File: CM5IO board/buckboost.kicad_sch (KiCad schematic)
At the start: 14 parts, among them IC1 TPS61089RNRR

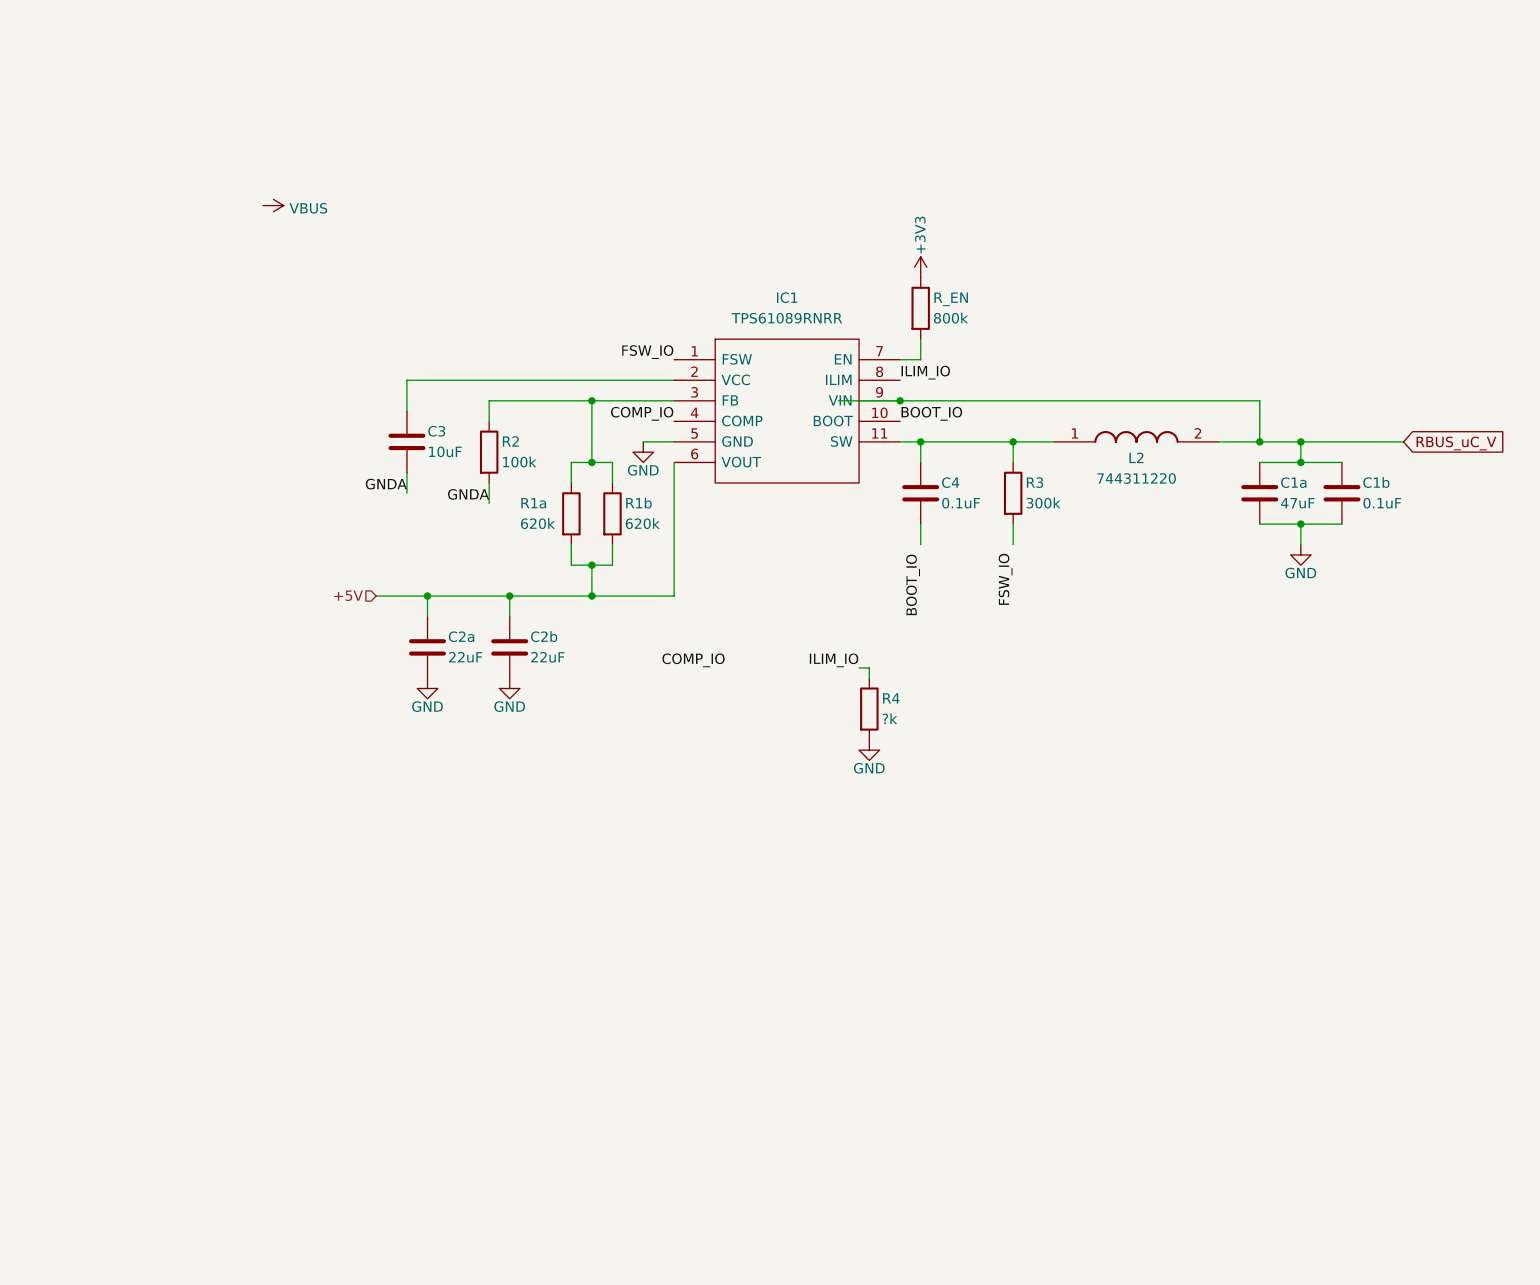
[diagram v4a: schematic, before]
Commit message: EN changed & finalised
Added MOSFET; using potential divider (i.e. R7//R8) EN switch is at 1.65V which is >1.2V from the data sheet. Added C7 to avoid voltage spikes.
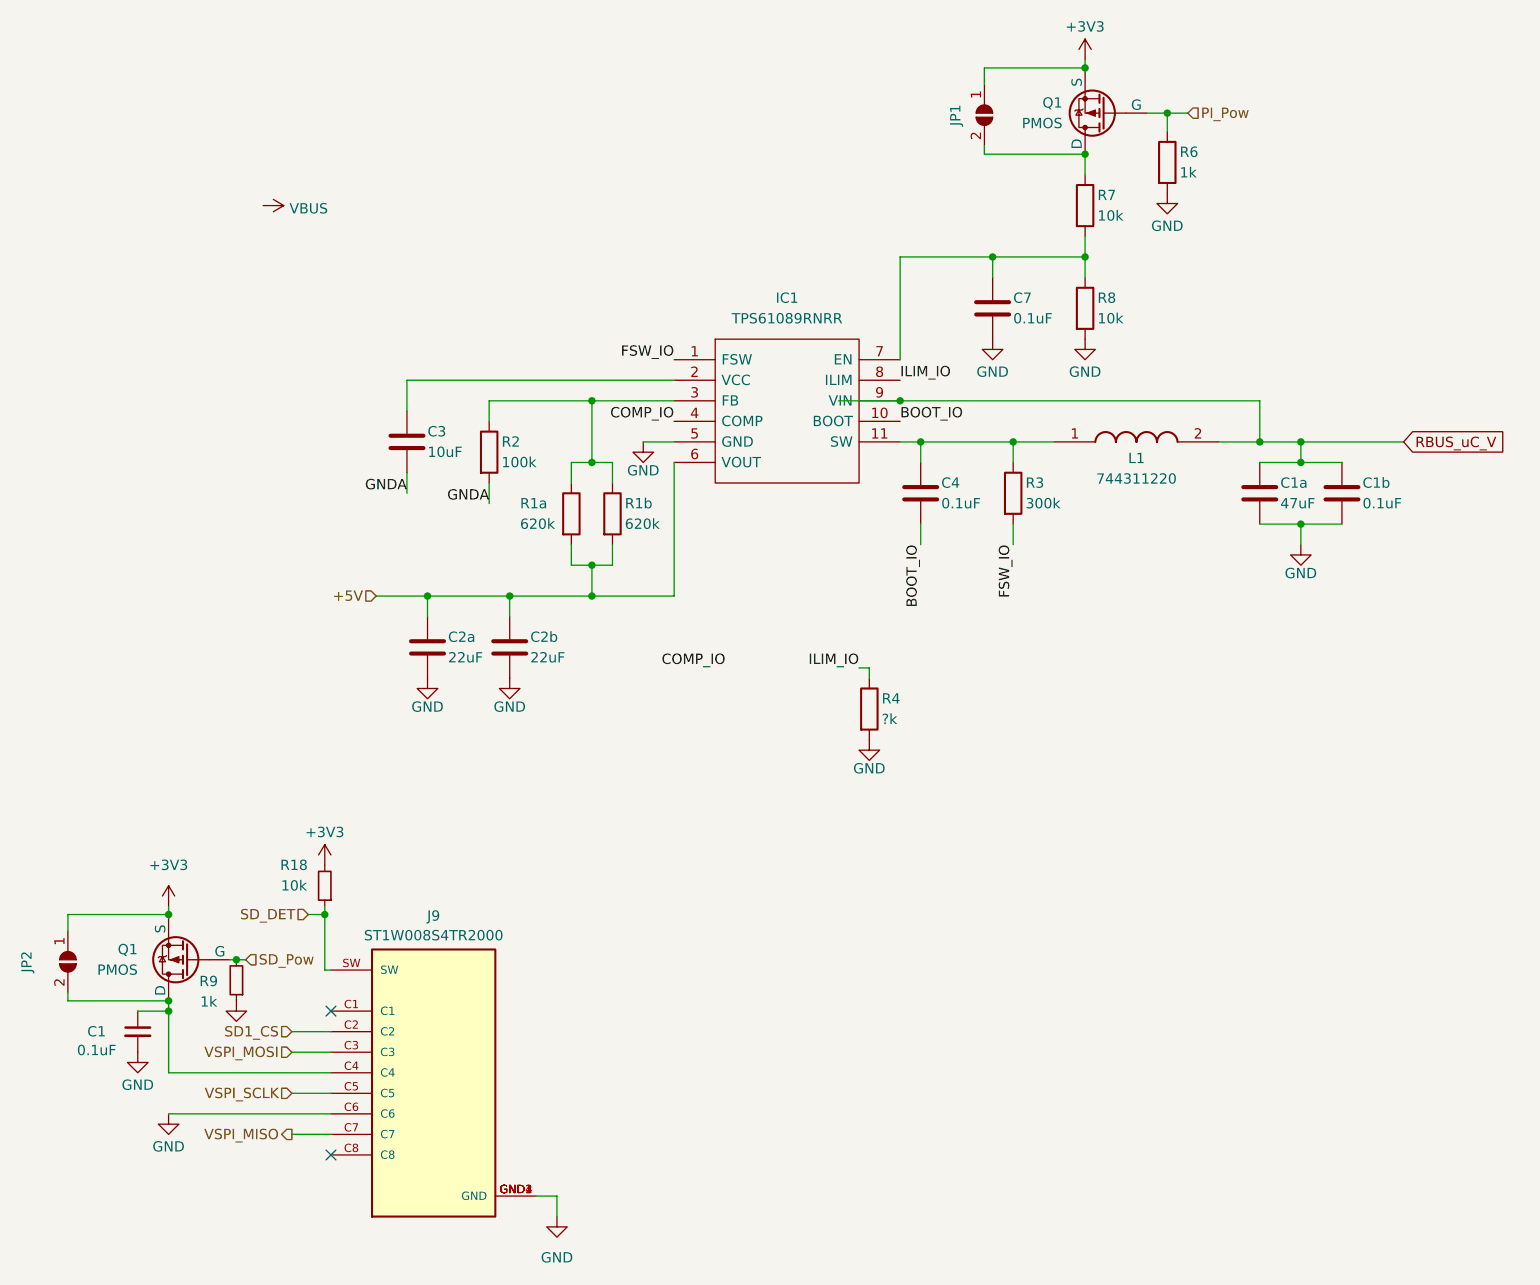
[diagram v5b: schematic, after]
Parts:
- removed R_EN: 800k, symbol Device:R
- added C1: 0.1uF, Capacitor_SMD:C_0402_1005Metric, symbol Device:C_Small
- added C7: 0.1uF, symbol Device:C
- added J9: ST1W008S4TR2000, iclr:JAE_ST1W008S4TR2000, symbol iclr:ST1W008S4TR2000
- added JP1, JP2: SolderJumper_2_Open, iclr:SmallerSolderJP, symbol Jumper:SolderJumper_2_Open
- added Q1 (x2): PMOS, Package_TO_SOT_SMD:SOT-23, symbol Simulation_SPICE:PMOS
- added R18: 10k, Resistor_SMD:R_0402_1005Metric, symbol Device:R_Small
- added R6: 1k, symbol Device:R
- added R7, R8: 10k, symbol Device:R
- added R9: 1k, Resistor_SMD:R_0402_1005Metric, symbol Device:R_Small
- renumbered L2 to L1
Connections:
- net +3V3: now also JP1.1 (A), JP2.1 (A), Q1.3 (S), Q1.3 (S), R18.2
- net BOOT_IO: now also C4.2
- net FSW_IO: now also R3.2
- net GND: now also C1.2, C7.2, J9.C6, J9.GND1 (GND), J9.GND2 (GND), J9.GND3 (GND), J9.GND4 (GND), R6.2, R8.2, R9.1
- net at IC1.7 (EN): now also C7.1, R7.2, R8.1
- new net: JP1.2 (B), Q1.1 (D), R7.1
- new net: C1.1, J9.C4, JP2.2 (B), Q1.1 (D)
- new net PI_Pow: Q1.2 (G), R6.1
- new net SD1_CS: J9.C2
- new net SD_DET: J9.SW, R18.1
- new net SD_Pow: Q1.2 (G), R9.2
- new net VSPI_MISO: J9.C7
- new net VSPI_MOSI: J9.C3
- new net VSPI_SCLK: J9.C5
- no-connect marks 0 -> 2

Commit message: COMP completed
η ≈ 85% | D = 0.45 | R_O = 1.67Ω | f_RHPZ = 36546 Hz | f_C ≈ 7 kHz | R5 = 6.2kΩ | C5 = 6 nF | R_ESR ≈ 0.05Ω | C6 = 360 pF
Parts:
- removed C1: 0.1uF, Capacitor_SMD:C_0402_1005Metric, symbol Device:C_Small
- removed J9: ST1W008S4TR2000, iclr:JAE_ST1W008S4TR2000, symbol iclr:ST1W008S4TR2000
- removed JP2: SolderJumper_2_Open, iclr:SmallerSolderJP, symbol Jumper:SolderJumper_2_Open
- removed Q1: PMOS, Package_TO_SOT_SMD:SOT-23, symbol Simulation_SPICE:PMOS
- removed R18: 10k, Resistor_SMD:R_0402_1005Metric, symbol Device:R_Small
- removed R9: 1k, Resistor_SMD:R_0402_1005Metric, symbol Device:R_Small
- added C5: 6nF, symbol Device:C
- added C6: 360pF, symbol Device:C
- added R5: 6.2k, symbol Device:R
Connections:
- net COMP_IO: now also C6.1, R5.1
- net GND: now also C5.2, C6.2
- new net: C5.1, R5.2
- no-connect marks 2 -> 0
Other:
- moved on the sheet: R4
